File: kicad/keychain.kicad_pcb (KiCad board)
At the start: 2 copper layers, 68.1 x 37.9 mm, 60 parts, among them J1 USB-C, J2 LiPo, J3 FPC-SMD_FH34SRJ-26S-0.5SH-50, Q1 BSS138, Q2 AO3401A, Q3 S8050, SW1 PWR, SW2 BOOT, SW3 USER, U1 ESP32-C6-MINI-1, U2 MCP73831, U3 AP2112K-3.3

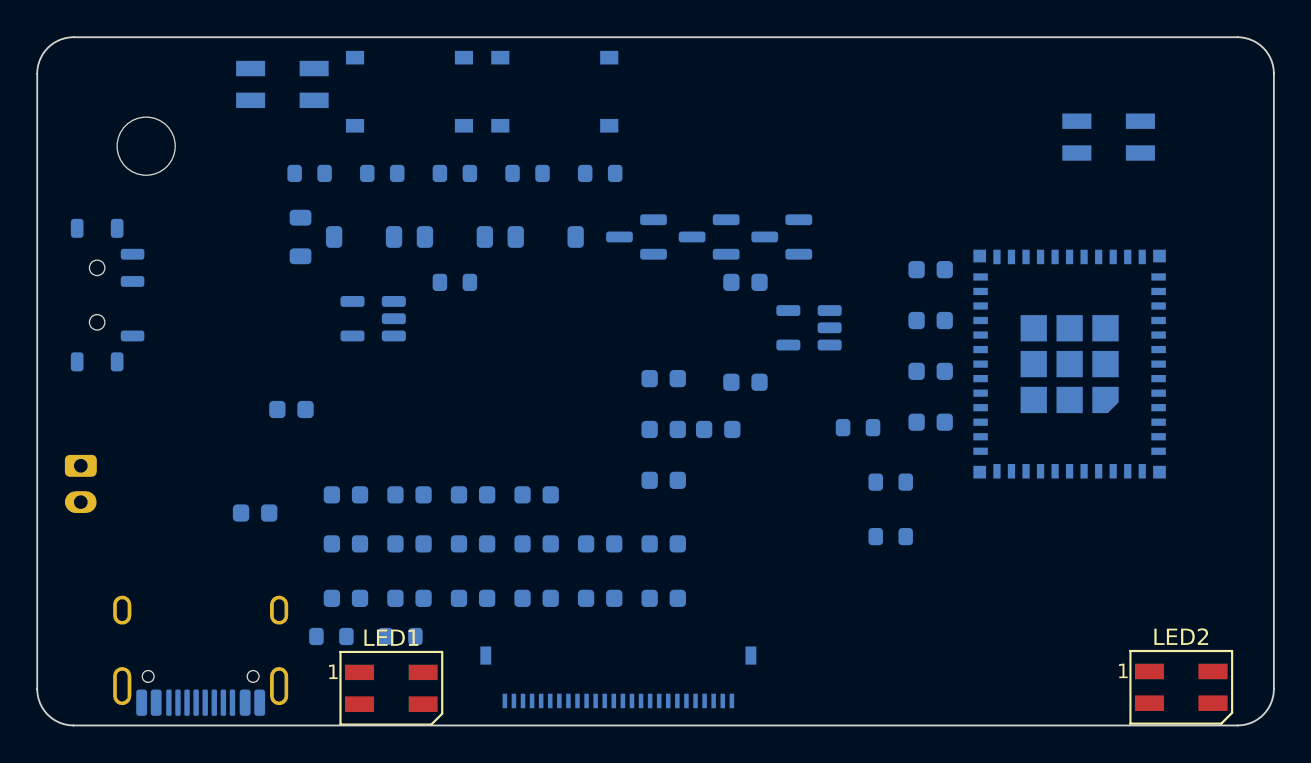
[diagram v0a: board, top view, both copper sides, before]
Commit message: Refine placement: decoupling/support parts next to their pins (no routing)
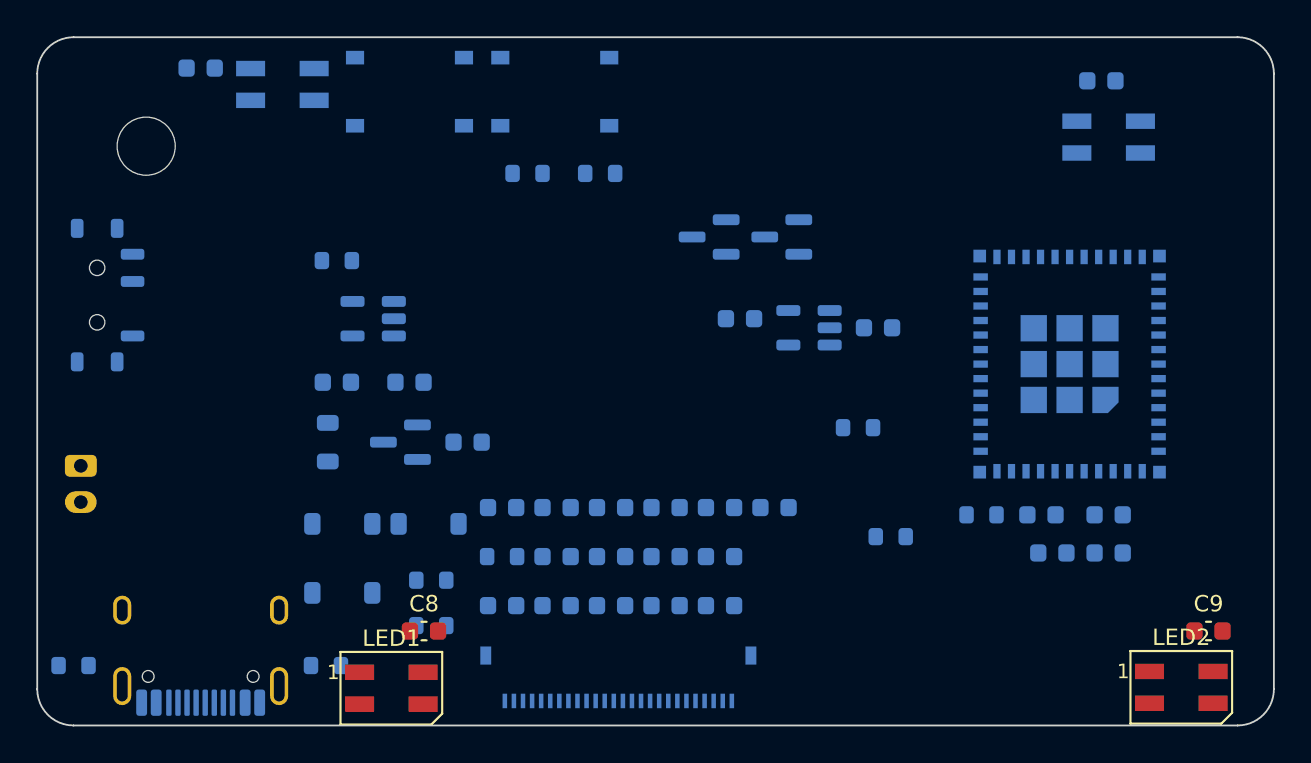
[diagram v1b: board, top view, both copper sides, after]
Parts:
- C8, C9: moved to F.Cu
- moved C10 34.8 mm to (39.0, 31.7)
- moved C11 32.6 mm to (88.6, 32.4)
- moved C9 32.0 mm to (94.5, 62.7), turned to 0 degrees
- moved R6 25.0 mm to (51.7, 62.4)
- moved R5 23.4 mm to (51.7, 59.9)
- moved D3 22.6 mm to (46.8, 60.6)
- moved R7 21.3 mm to (55.6, 58.6)
- moved C14 21.2 mm to (67.6, 55.9)
- moved C21 20.2 mm to (70.6, 55.9)
- moved C8 19.2 mm to (51.3, 62.7), turned to 0 degrees
- moved Q1 17.2 mm to (50.0, 52.3)
- moved C5 17.0 mm to (85.9, 58.4)
- moved D2 15.9 mm to (51.5, 56.8)
- moved D1 15.8 mm to (46.8, 56.8)
- moved C26 15.8 mm to (61.6, 61.3)
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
